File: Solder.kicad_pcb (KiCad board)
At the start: 2 copper layers, 135.9 x 275.4 mm, 6 parts

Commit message: Add random bits
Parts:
- moved G*** 1.12 mm to (129.5, 75.0), turned to -12 degrees
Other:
- board text added: "Fishhhhhhhhhhh"
- board text added: "Hacklet is the BEST ysws!"

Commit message: More random text... (hopefully not too small to print)
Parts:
- removed the G*** at (129.5, 75.0)
- added G***: LOGO, LOGO, F.Cu at (127.5, 45.5)
- added G***: LOGO, LOGO, B.Cu at (124.5, 59.0)
- added G***: LOGO, LOGO, B.Cu at (94.2, 59.5)
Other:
- board text added: "(You should join Hack Club)"
- board text added: "Fishhhhhhhhh"
- board text added: "Hi!"
- board text added: "Made for Hack Club's"
- board text added: "dQw4w9WgXcQ"
- board text removed: "Fishhhhhhhhhhh"

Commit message: add ground pour
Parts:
- removed the G*** at (127.5, 45.5)
- moved G*** 1.06 mm to (93.5, 60.2)
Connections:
- net Net-(BT1-+) renamed GND
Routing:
- net GND: track 70.3 -> 3.87 mm
- added copper zone on B.Cu, net GND
- added copper zone on F.Cu, net GND
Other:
- board text added: "(Also, Hacklet is the BEST ysws!)"
- board text removed: "Hacklet is the BEST ysws!"

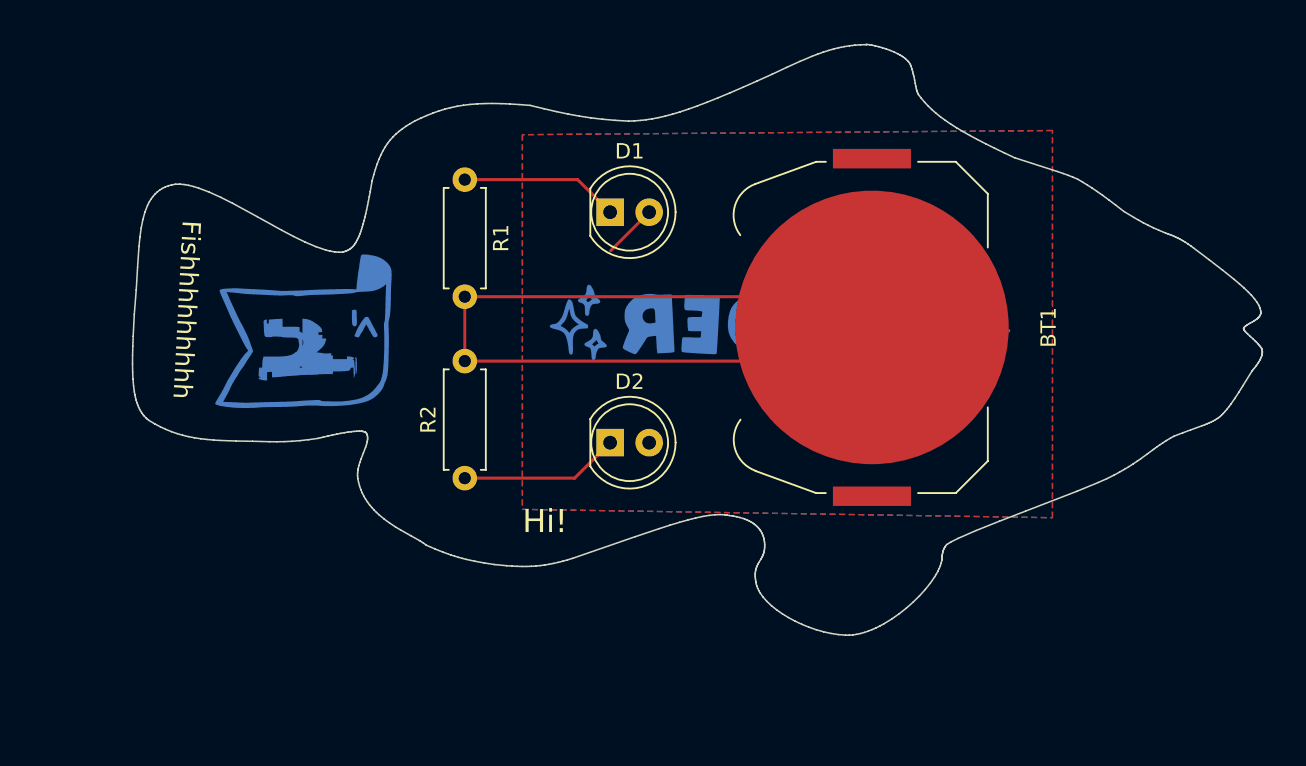
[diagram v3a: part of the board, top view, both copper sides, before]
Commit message: Ground fill EVERYTHING
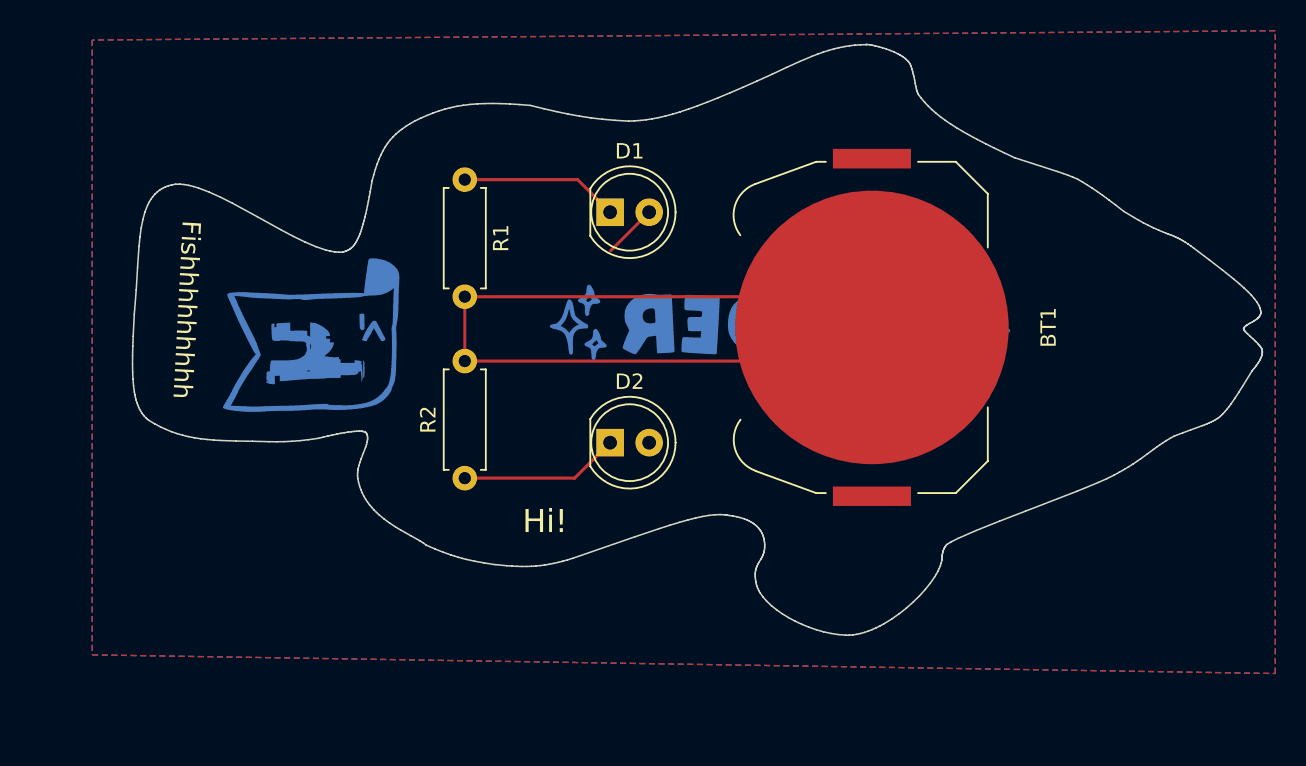
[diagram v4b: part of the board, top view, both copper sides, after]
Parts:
- moved G*** 0.56 mm to (94.0, 60.5)
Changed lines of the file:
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@@
 	(footprint "LOGO"
 		(layer "B.Cu")
-		(at 93.5 60.25 90)
+		(at 94 60.5 90)
 		(property "Reference" "G***"
 			(at 0 0 90)
@@
 	)
 	(gr_text "(Also, Hacklet is the BEST ysws!)"
-		(at 100.75 72.5 270)
+		(at 101 72.75 270)
 		(layer "B.SilkS")
 		(effects
@@
 		(min_thickness 0.25)
 		(filled_areas_thickness no)
-		(fill
+		(fill yes
 			(thermal_gap 0.5)
 			(thermal_bridge_width 0.5)
@@
 		(polygon
 			(pts
-				(xy 142.25 47.18307) (xy 107.75 47.454725) (xy 107.75 71.840551) (xy 142.25 72.383858)
-			)
-		)
+				(xy 156.75 40.688985) (xy 79.75 41.295287) (xy 79.75 81.311026) (xy 156.75 82.523623)
+			)
+		)
